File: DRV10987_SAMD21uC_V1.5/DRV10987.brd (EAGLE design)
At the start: 96.2 x 90 mm, 75 parts, among them J1 SUCHAI_PCB, J10 455-1750-1-ND, J7 MK1_ZERO_ZX62AB-5PA(11), U1 MK1_ZERO_AP7215-33YG-13, U2 ATSAMD21G-A, Y1 32.768kHz

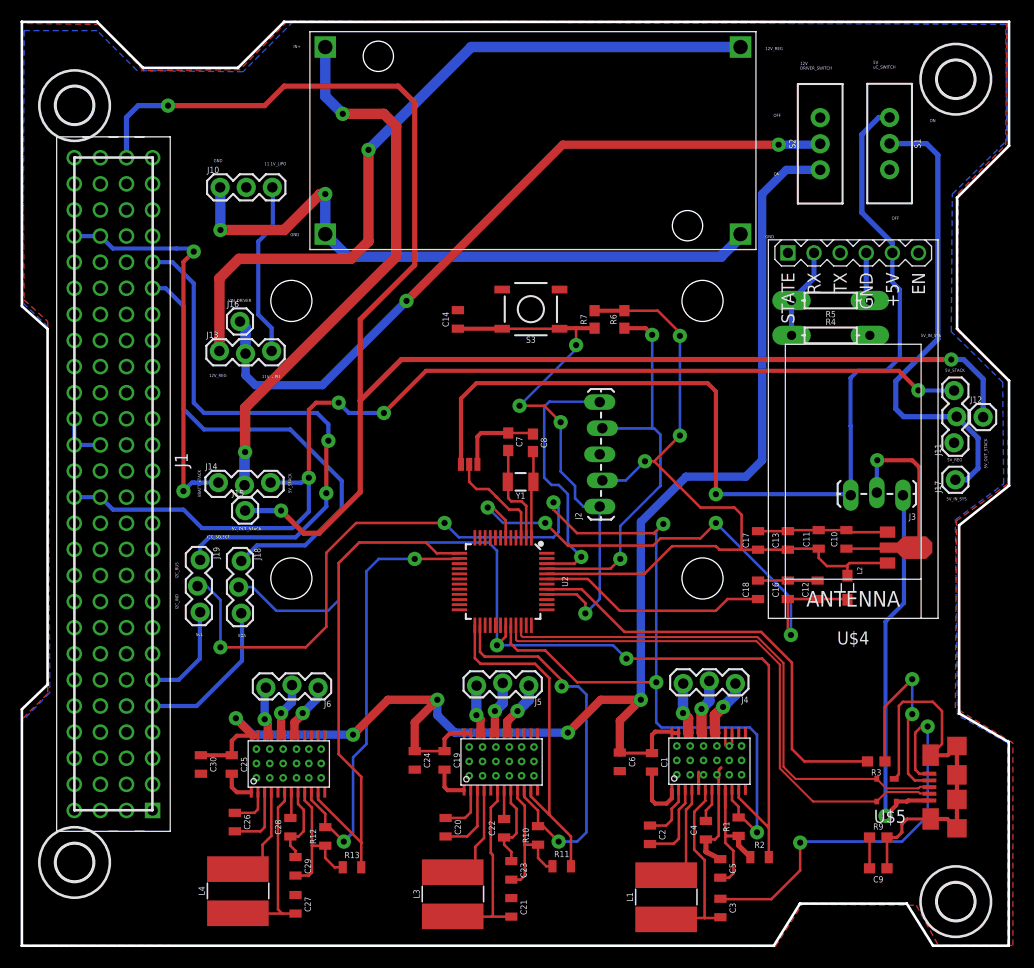
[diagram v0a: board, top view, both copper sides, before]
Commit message: new SAMD21uC_v1.5, added BTS5045, molex connectors, remove conf jumpers, and added holes for wires
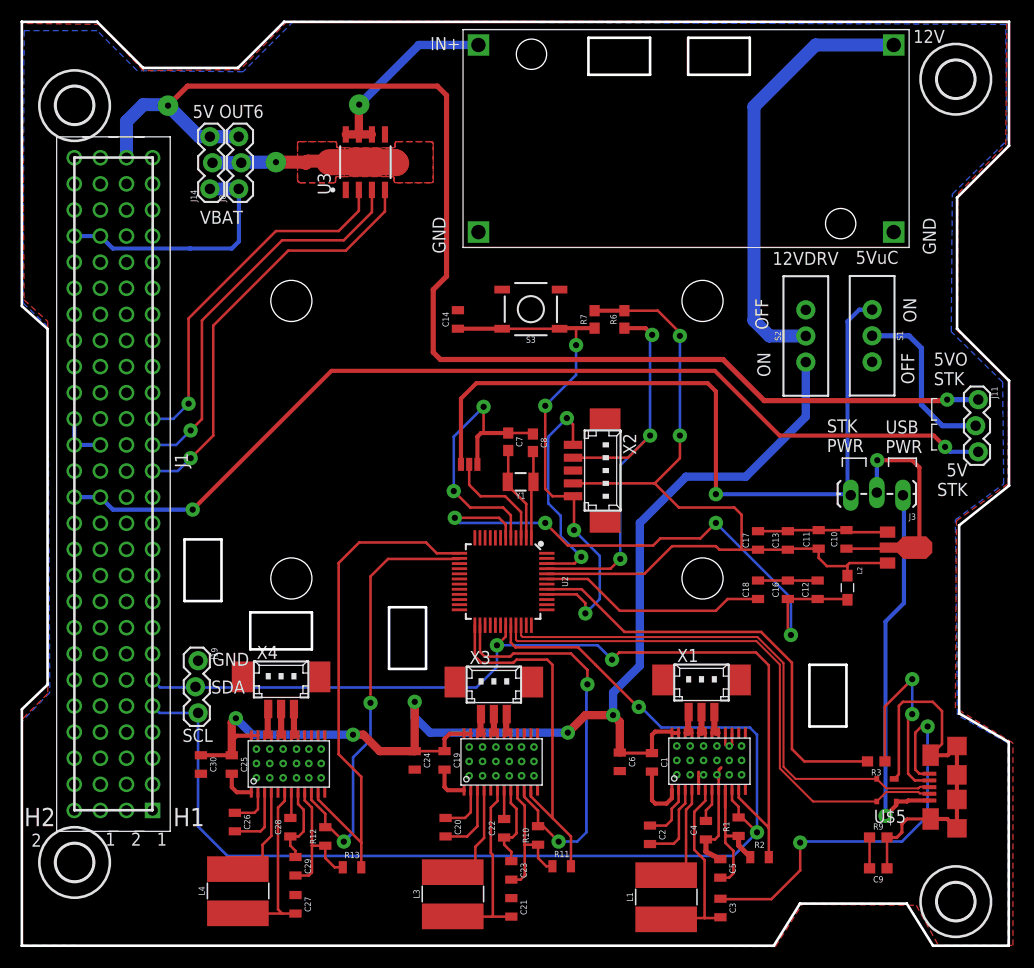
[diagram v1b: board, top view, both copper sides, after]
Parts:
- removed J10: 455-1750-1-ND, SparkFun-Connectors:1X03
- removed J12, J15, J16, J17: (no value), SparkFun-Connectors:1X01
- removed J13, J18, J4, J5, J6: (no value), SparkFun-Connectors:1X03_LOCK
- removed J2: (no value), SparkFun-Connectors:1X05_LOCK_LONGPADS
- removed R4: 1k, resistors-longpads:AXIAL-0.3
- removed R5: 2k, resistors-longpads:AXIAL-0.3
- removed U$4: WIRELESS-BLUETOOTH-HC-05-MIRRORMIRROR, diy-modules:WIRELESS-BLUETOOTH-HC-05-MIRROR
- added J8: (no value), SparkFun-Connectors:1X03_LOCK
- added U3: BTS5045-1EJA, BTS5045-1EJA:SOIC127P600X170-9N
- added X1, X3, X4: 53398-03, con-molex:53398-03
- added X2: 53398-05, con-molex:53398-05
- moved J14 28.7 mm to (-90.8, 74.9), turned to 90 degrees
- moved S1 18.8 mm to (-26.5, 60.6)
- moved S2 18.8 mm to (-33.0, 60.6)
- moved U$2 14.9 mm to (-66.3, 69.2)
- moved J19 9.80 mm to (-92.2, 29.0)
- moved J11 4.70 mm to (-16.3, 54.4), turned to 270 degrees
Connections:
- removed net 11.1V_LIPO: J10.3, J13.3
- removed net I2C2_SCL: J1.6, J19.3
- removed net I2C2_SDA: J1.5, J18.3
- removed net I2C_SCL: J1.22, J19.1
- removed net I2C_SDA: J1.21, J18.1
- removed net MCU-RX: U$4.3
- removed net MCU-TX: R4.P$2
- removed net N$13: R4.P$1, R5.P$2, U$4.2
- new net BTS_VS: J14.2, J8.2, U3.9
- new net N$12: U$2.IN+, U3.6, U3.7, U3.8
- new net RWS_DEN: J1.15, U3.3
- new net RWS_EN: J1.16, U3.2
- new net RWS_IS: J1.14, U3.4
- net +5V: no longer U$4.5
- net 12V_REG: now also S2.2; no longer J13.1
- net 3V3: now also X2.2; no longer J2.2
- net 5V_OUT_STACK: now also J11.1, J14.3, J8.3; no longer J12.1, J15.1
- net 5V_STACK: no longer J14.3
- net GND: now also J19.1, U3.1, X2.3; no longer J10.1, J2.3, R5.P$1, U$4.4
- net I2C_SCL_UC: now also J1.5, J19.3; no longer J19.2
- net I2C_SDA_UC: now also J1.6, J19.2; no longer J18.2
- net N$16: now also J1.21; no longer J13.2, J16.1, S2.2
- net N$18: now also J1.22; no longer J14.2, U$2.IN+
- net N$5: no longer J17.1
- net OUT1: now also X1.1; no longer J4.1
- net OUT1_M2: now also X3.1; no longer J5.1
- net OUT1_M3: now also X4.1; no longer J6.1
- net OUT2: now also X1.2; no longer J4.2
- net OUT2_M2: now also X3.2; no longer J5.2
- net OUT2_M3: now also X4.2; no longer J6.2
- net OUT3: now also X1.3; no longer J4.3
- net OUT3_M2: now also X3.3; no longer J5.3
- net OUT3_M3: now also X4.3; no longer J6.3
- net RESET: now also X2.1; no longer J2.1
- net SWCLK: now also X2.4; no longer J2.4
- net SWDIO: now also X2.5; no longer J2.5
- net V_BATT_STACK: now also J8.1
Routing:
- net N$16: track 71.5 -> 0.00 mm, vias 2 -> 0
- net N$18: track 53.9 -> 0.00 mm, vias 2 -> 0
- net I2C_SCL: track 53.7 -> 0.00 mm, vias 2 -> 0
- net I2C_SDA: track 46.9 -> 0.00 mm
- net GND: track 170.5 -> 124.3 mm
- net RWS_IS: track 0.00 -> 41.4 mm, vias 0 -> 1
- net RWS_DEN: track 0.00 -> 38.5 mm, vias 0 -> 1
- net RWS_EN: track 0.00 -> 35.3 mm, vias 0 -> 1
- net 12V_REG: track 72.3 -> 42.6 mm, vias 1 -> 0
- net 5V_OUT_STACK: track 154.7 -> 125.2 mm, vias 3 -> 2
- net N$5: track 46.4 -> 16.9 mm
- net 12V: track 145.1 -> 120.4 mm
- net +5V: track 99.0 -> 75.2 mm
- net BTS_VS: track 0.00 -> 21.6 mm, vias 0 -> 1
- net N$12: track 0.00 -> 19.5 mm, vias 0 -> 1
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- added copper zone on layer 1, net BTS_VS
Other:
- board text added: "1"
- board text added: "12V"
- board text added: "12VDRV"
- board text added: "2"
- board text added: "5V OUT6"
- board text added: "5V STK"
- board text added: "5VO STK"
- board text added: "5VuC"
- board text added: "H1"
- board text added: "H2"
- board text added: "STK PWR"
- board text added: "USB PWR"
- board text added: "VBAT"
- board text removed: "11.1V_LIPO"
- board text removed: "11V_LIPO"
- board text removed: "12V DRIVER_SWITCH"
- board text removed: "12V_REG"
- board text removed: "5V uC_SWITCH"
- board text removed: "5V_IN_SYS"
- board text removed: "5V_OUT_STACK"
- board text removed: "5V_REG"
- board text removed: "5V_STACK"
- board text removed: "I2C_BUS"
- board text removed: "I2C_IND"
- board text removed: "I2C_SELECT"
- board text removed: "VBATT_STACK"
- board text removed: "VIN_DRIVER"

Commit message: added rtc, atmega328, leds, labels and adjust usb connector
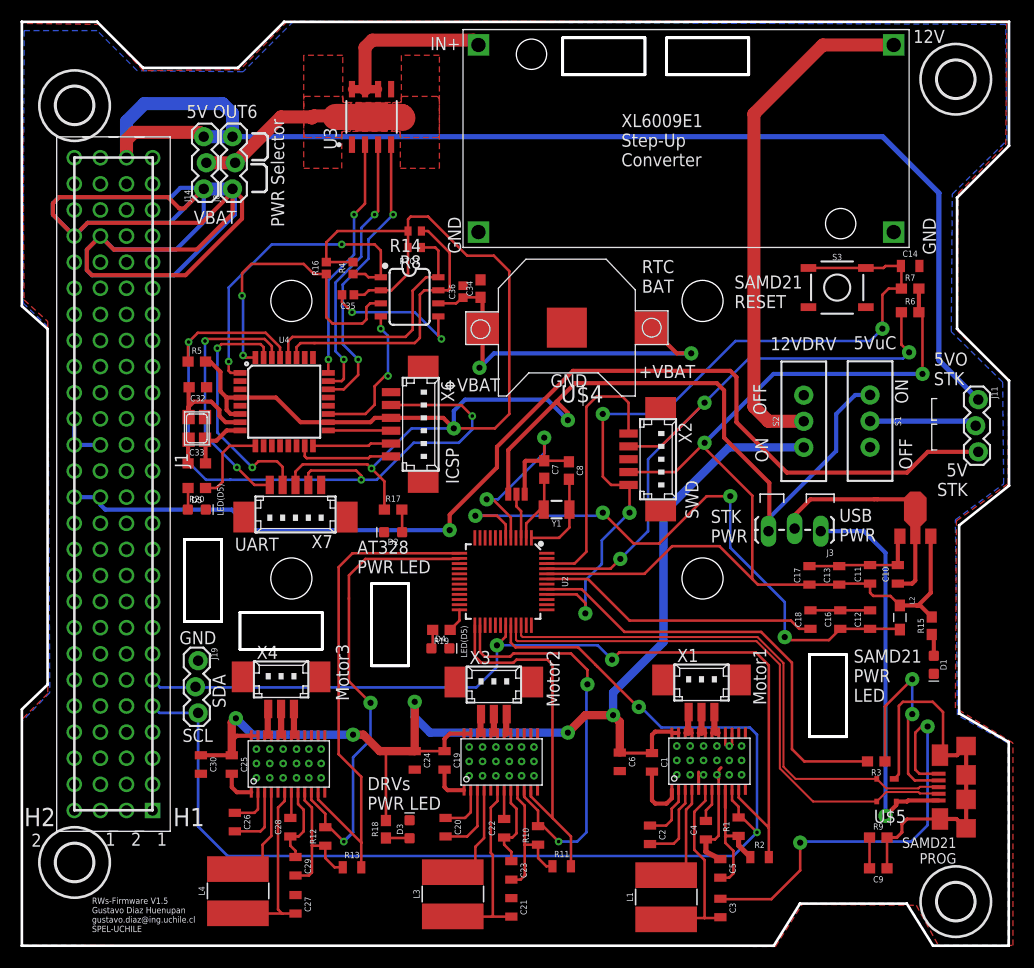
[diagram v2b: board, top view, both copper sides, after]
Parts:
- added C32, C33: 22pF, SparkFun-Capacitors:0603
- added C34: 1nF, SparkFun-Capacitors:0603
- added C35, C36: 1.0uF, SparkFun-Capacitors:0402
- added D1: RED, SparkFun-LED:LED-0603
- added D2, D4, D5: BLUE, SparkFun-LED:LED-0603
- added D3: GREEN, SparkFun-LED:LED-0603
- added Q2: (no value), adafruit:NX3225
- added R14, R8: (no value), adafruit:R0402
- added R15, R17, R19, R20: 22, SparkFun-Resistors:0603
- added R16, R4: 100K, SparkFun-Resistors:0402
- added R18: 1k, SparkFun-Resistors:0603
- added R5: 10k, SparkFun-Resistors:0603
- added RTC1: DS3231M, SparkFun-Clocks:SO08
- added U$4: (no value), adafruit:CR1220-SMD
- added U4: ATMEGA328P_TQFP, SparkFun-IC-Microcontroller:TQFP32-08
- added X6: 53398-06, con-molex:53398-06
- added X7: 53398-05, con-molex:53398-05
- moved C14 44.3 mm to (-22.8, 67.4), turned to 0 degrees
- moved R7 30.8 mm to (-22.8, 65.2), turned to 0 degrees
- moved S3 29.9 mm to (-29.9, 65.3), turned to 0 degrees
- moved R6 27.8 mm to (-22.8, 62.9), turned to 0 degrees
- moved J3 8.73 mm to (-31.5, 41.6)
- moved S2 8.30 mm to (-33.1, 52.3)
- moved S1 8.30 mm to (-26.7, 52.3)
- moved C13 6.05 mm to (-29.7, 37.3)
- moved C17 6.05 mm to (-32.6, 37.3)
- moved C10 6.05 mm to (-24.0, 37.4)
- moved C11 6.05 mm to (-26.7, 37.4)
- moved C12 5.87 mm to (-26.7, 33.0)
- moved C16 5.87 mm to (-29.6, 33.0)
- moved C18 5.87 mm to (-32.5, 33.0)
- moved L2 5.87 mm to (-23.8, 33.2)
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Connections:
- new net AT328-RX: U4.30, X7.1
- new net AT328-TX: U4.31, X7.2
- new net AT328_MISO: U4.16, X6.2
- new net AT328_MOSI: U4.15, X6.1
- new net AT328_RESET: R5.1, U4.29, X6.5, X7.4
- new net AT328_SCK: U4.17, X6.3
- new net N$13: C32.2, Q2.1, U4.7
- new net N$14: C33.2, Q2.3, U4.8
- new net N$15: D1.A, R15.1
- new net N$21: D2.A, R17.2
- new net N$36: D3.A, R18.1
- new net N$37: D4.A, R19.2
- new net N$38: R19.1, U2.24
- new net N$39: D5.A, R20.2
- new net N$40: R20.1, U4.9
- new net RTC_32KHZ: R4.1, RTC1.1, U4.1
- new net RTC_BAT: C34.1, C36.1, RTC1.6, U$4.+$1, U$4.+$2
- new net RTC_INT: R16.1, RTC1.3, U4.32
- new net RTC_RST: RTC1.4, U4.19
- new net RTC_SCL: R8.1, RTC1.8, U4.28
- new net RTC_SDA: R14.1, RTC1.7, U4.27
- net +5V: now also C35.1, R14.2, R16.2, R17.1, R4.2, R5.2, R8.2, RTC1.2, U4.18, U4.4, U4.6, X6.4, X7.3
- net 12V: now also R18.2
- net 3V3: now also R15.2
- net GND: now also C32.1, C33.1, C34.2, C35.2, C36.2, D1.C, D2.C, D3.C, D4.C, D5.C, Q2.2, Q2.4, RTC1.5, U$4.-, U4.3, U4.5, X6.6, X7.5
- net RWS_DEN: now also U4.23; no longer J1.15
- net RWS_EN: now also U4.24; no longer J1.16
- net RWS_IS: now also U4.22; no longer J1.14
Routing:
- net V_BATT_STACK: track 24.7 -> 154.8 mm
- net +5V: track 75.2 -> 189.0 mm, vias 1 -> 3
- net AT328_RESET: track 0.00 -> 71.5 mm, vias 0 -> 3
- net RTC_BAT: track 0.00 -> 37.5 mm, vias 0 -> 2
- net RTC_32KHZ: track 0.00 -> 31.5 mm, vias 0 -> 2
- net RTC_INT: track 0.00 -> 29.6 mm, vias 0 -> 2
- net RTC_SDA: track 0.00 -> 27.8 mm
- net AT328-RX: track 0.00 -> 25.5 mm, vias 0 -> 2
- net RTC_SCL: track 0.00 -> 25.4 mm
- net RESET: track 51.4 -> 75.7 mm
- net AT328-TX: track 0.00 -> 24.0 mm, vias 0 -> 2
- net 3V3: track 82.7 -> 105.4 mm
- net SWCLK: track 42.0 -> 61.4 mm
- net RTC_RST: track 0.00 -> 14.5 mm, vias 0 -> 2
- net RWS_IS: track 41.4 -> 28.6 mm, vias 1 -> 2
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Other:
- board text added: "+VBAT"
- board text added: "AT328 PWR LED"
- board text added: "DRVs PWR LED"
- board text added: "ICSP"
- board text added: "LED(D5)"
- board text added: "Motor1"
- board text added: "Motor2"
- board text added: "Motor3"
- board text added: "PWR Selector"
- board text added: "RTC BAT"
- board text added: "RWs-Firmware V1.5 Gustavo Diaz Huenupan gustavo.diaz@ing.uchile.cl SPEL-UCHILE"
- board text added: "SAMD21 PROG"
- board text added: "SAMD21 PWR LED"
- board text added: "SAMD21 RESET"
- board text added: "SWD"
- board text added: "UART"
- board text added: "XL6009E1 Step-Up Converter"
